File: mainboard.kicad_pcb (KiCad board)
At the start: 2 copper layers, 145 x 95 mm, 140 parts, among them J1 USB_C_Receptacle_USB2.0_16P, J10 Valve7, J11 AuxPump, J12 MainPump, J13 WaterLevelSensor, J14 OneWireTemp, J15 OneWireTemp, J2 Valve1, J3 Servo, J4 HX711, J5 Valve2, J6 Valve3, J7 Valve4, J8 Valve5, J9 Valve6, Q1 DMN3008SFG, Q10 IRLML2502, Q11 IRLML2502, Q2 DMN3008SFG, Q3 IRLML2502, Q4 IRLML2502, Q5 IRLML2502, Q6 IRLML2502, Q7 IRLML2502, Q8 IRLML2502, Q9 IRLML2502, SW1 SW_Push, SW2 SW_Push, SW3 SW_Push, U1 AP33771, U2 AP62150WU, U3 DRV8870DDAR, U4 AP62150WU, U5 USBLC6-2SC6, U6 ESP32-S3-WROOM-1

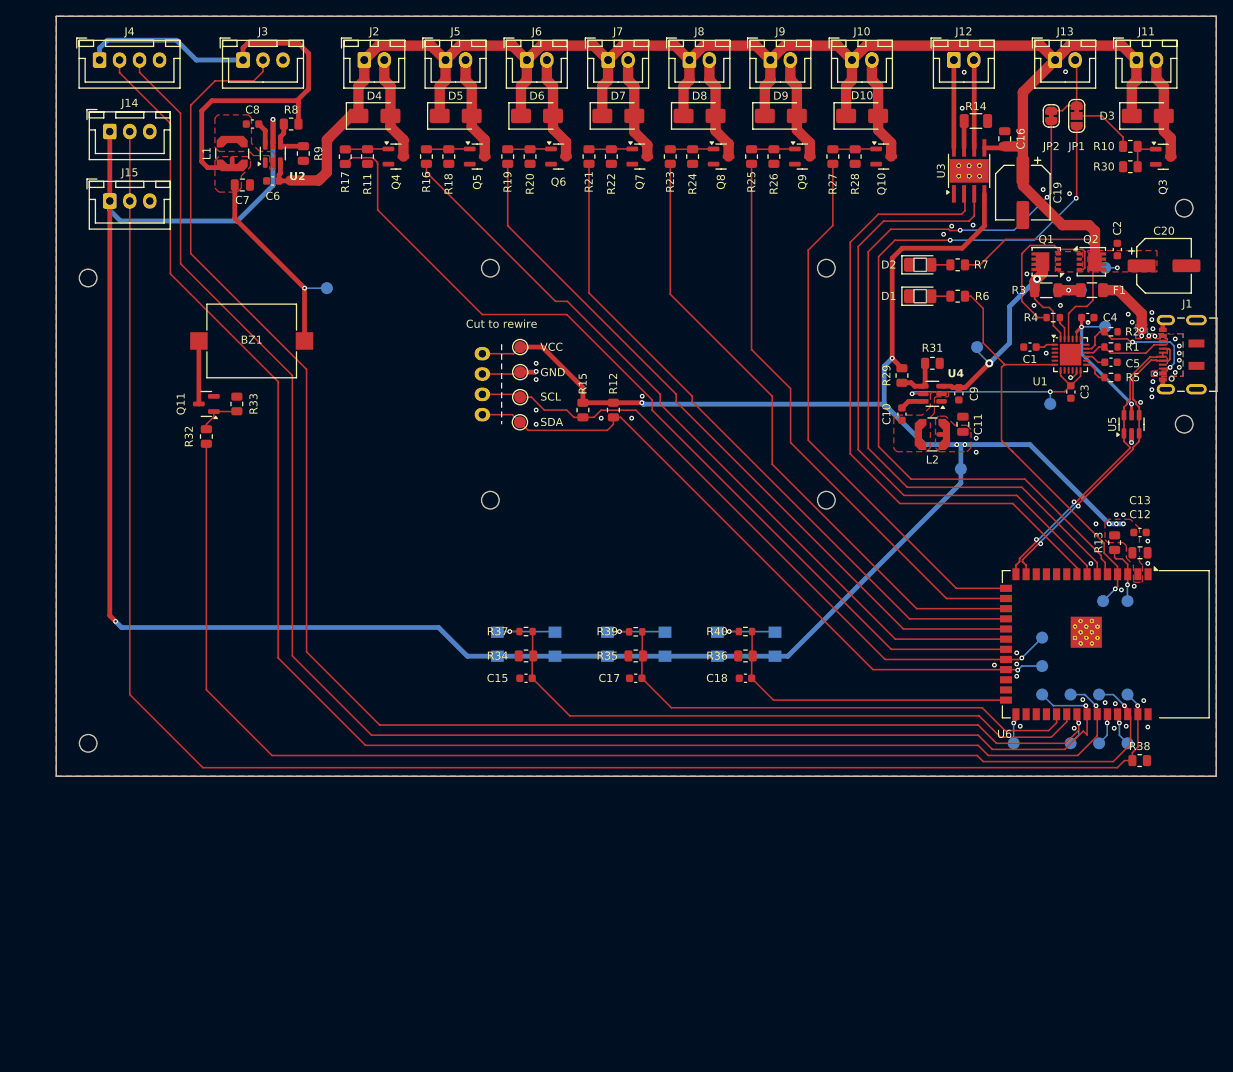
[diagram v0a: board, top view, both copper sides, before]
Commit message: Cleanup OLED stuff
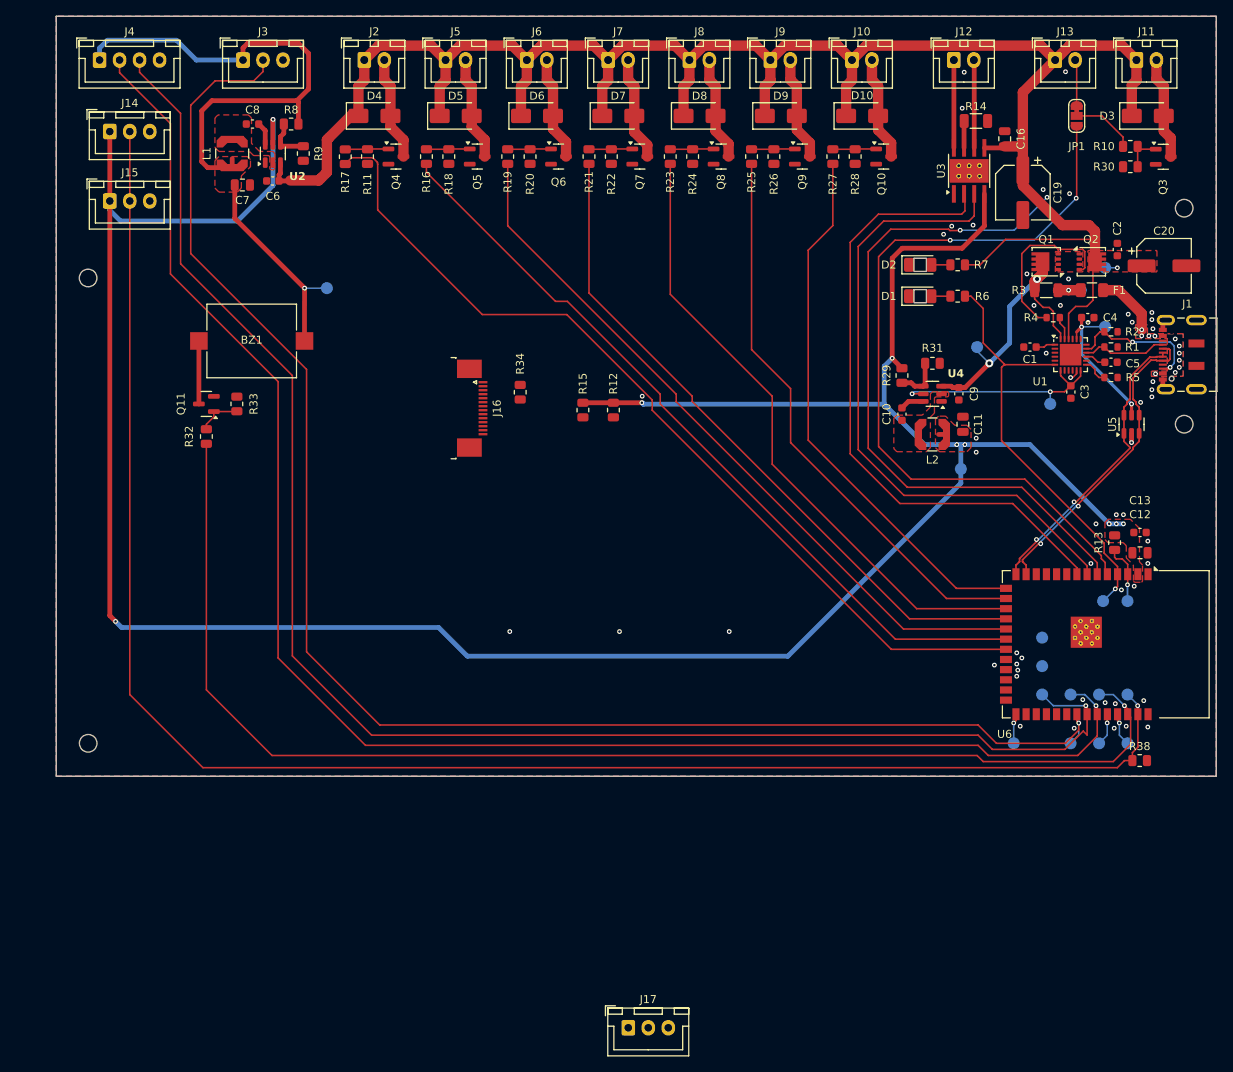
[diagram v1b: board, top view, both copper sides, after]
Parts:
- removed C15, C17, C18: 100n, Capacitor_SMD:C_0603_1608Metric
- removed JP2: SolderJumper_2_Bridged, Jumper:SolderJumper-2_P1.3mm_Bridged_RoundedPad1.0x1.5mm
- removed R35, R36: R100k, Resistor_SMD:R_0805_2012Metric
- removed R37, R39, R40: 1k, Resistor_SMD:R_0603_1608Metric
- removed SW1, SW2, SW3: SW_Push, Button_Switch_SMD:SW_SPST_TL3305A
- removed TP1, TP2, TP3, TP4: TestPoint_Small, TestPoint:TestPoint_Pad_D1.5mm
- removed U8: ~, project:OLED_1.5in_128x128
- added J16: Conn_01x14_MountingPin, Connector_FFC-FPC:TE_1-1734839-4_1x14-1MP_P0.5mm_Horizontal, F.Cu at (103.0, 78.0)
- added J17: FlowSensor, Connector_JST:JST_XH_B3B-XH-A_1x03_P2.50mm_Vertical, F.Cu at (122.5, 155.4)
- moved R34 33.0 mm to (109.0, 76.0), turned to -90 degrees
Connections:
- net /MCU/WATER_LEVEL_SENSOR renamed /Motor Control/WATER_LEVEL_SENSOR
- R12 pad 2: /MCU/OLED_SDA -> /MCU/LCD_TOUCH_SDA
- R15 pad 2: /MCU/OLED_SCL -> /MCU/LCD_TOUCH_SCL
- R34 pad 2: /MCU/BUTTON_1 -> /User Interface/LCD_CS
- TP7 pad 1: /MCU/OLED_SCL -> Net-(U6-IO14)
- TP8 pad 1: /MCU/OLED_SDA -> Net-(U6-IO21)
- U6 pad 22: /MCU/OLED_SCL -> Net-(U6-IO14)
- U6 pad 23: /MCU/OLED_SDA -> Net-(U6-IO21)
- U6 pad 26: /MCU/BUTTON_3 -> unconnected-(U6-IO45-Pad26)
- U6 pad 31: /MCU/BUTTON_2 -> unconnected-(U6-IO38-Pad31)
- U6 pad 32: /MCU/BUTTON_1 -> unconnected-(U6-IO39-Pad32)
- U6 pad 6: /MCU/WATER_LEVEL_SENSOR_PIN -> /MCU/FLOW_SENSOR
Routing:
- net /MCU/WATER_LEVEL_SENSOR_PIN: track 95.6 -> 0.00 mm, vias 2 -> 0
- net /MCU/FLOW_SENSOR: track 0.00 -> 85.9 mm, vias 0 -> 2
- net /MCU/OLED_SDA: track 85.3 -> 0.00 mm, vias 1 -> 0
- net /MCU/OLED_SCL: track 85.1 -> 0.00 mm, vias 1 -> 0
- net /MCU/BUTTON_1: track 77.2 -> 0.00 mm
- net /MCU/BUTTON_2: track 61.6 -> 0.00 mm
- net /MCU/BUTTON_3: track 38.5 -> 0.00 mm
- net +3.3V: track 348.1 -> 331.2 mm
- net Net-(R39-Pad1): track 8.25 -> 0.00 mm, vias 1 -> 0
- net Net-(R40-Pad1): track 8.24 -> 0.00 mm, vias 1 -> 0
- net Net-(R37-Pad1): track 8.24 -> 0.00 mm, vias 1 -> 0
- net GND: track 11.8 -> 5.28 mm, vias 56 -> 49
- net /Motor Control/WATER_LEVEL_SENSOR: track 8.94 -> 5.49 mm
- net (no net): vias 0 -> 5
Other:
- board text removed: "Check pinout!!!"
- board text removed: "Cut to rewire"
- board text removed: "GND"
- board text removed: "SCL"
- board text removed: "SDA"
- board text removed: "VCC"

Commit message: Cleanup
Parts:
- added TP1: TestPoint_Small, TestPoint:TestPoint_Pad_D1.5mm, F.Cu at (164.3, 150.4)
- added TP15: TestPoint_Small, TestPoint:TestPoint_Pad_D1.5mm, F.Cu at (171.4, 150.4)
- added TP2: TestPoint_Small, TestPoint:TestPoint_Pad_D1.5mm, F.Cu at (164.3, 154.0)
- added TP23: TestPoint_Small, TestPoint:TestPoint_Pad_D1.5mm, F.Cu at (171.4, 154.0)
- added TP24: TestPoint_Small, TestPoint:TestPoint_Pad_D1.5mm, F.Cu at (175.0, 150.4)
- added TP27: TestPoint_Small, TestPoint:TestPoint_Pad_D1.5mm, F.Cu at (175.0, 154.0)
- added TP3: TestPoint_Small, TestPoint:TestPoint_Pad_D1.5mm, F.Cu at (167.9, 150.4)
- added TP4: TestPoint_Small, TestPoint:TestPoint_Pad_D1.5mm, F.Cu at (167.9, 154.0)
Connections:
- J16 pad 7: /MCU/LCD_MISO -> /MCU/LCD_SCK
- J16 pad 8: /MCU/LCD_SCK -> /User Interface/LCD_BACKLIGHT
- J16 pad 9: /User Interface/LCD_LED_K -> /MCU/LCD_MISO
- TP7 pad 1: Net-(U6-IO14) -> /MCU/LCD_SCK
- TP8 pad 1: Net-(U6-IO21) -> /MCU/LCD_TOUCH_RESET
- U6 pad 10: unconnected-(U6-IO17-Pad10) -> /MCU/LCD_MOSI
- U6 pad 11: unconnected-(U6-IO18-Pad11) -> /MCU/LCD_MISO
- U6 pad 12: unconnected-(U6-IO8-Pad12) -> /MCU/LCD_RS
- U6 pad 22: Net-(U6-IO14) -> /MCU/LCD_SCK
- U6 pad 23: Net-(U6-IO21) -> /MCU/LCD_TOUCH_RESET
- U6 pad 26: unconnected-(U6-IO45-Pad26) -> /MCU/LCD_TOUCH_INT
- U6 pad 31: unconnected-(U6-IO38-Pad31) -> /MCU/LCD_TOUCH_SDA
- U6 pad 32: unconnected-(U6-IO39-Pad32) -> /MCU/LCD_TOUCH_SCL
- U6 pad 9: unconnected-(U6-IO16-Pad9) -> /MCU/LCD_RESET
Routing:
- net /MCU/HX711_CLK: track 199.0 -> 4.88 mm
- net /MCU/1WIRE_TEMP: track 208.9 -> 17.8 mm
- net /MCU/HX711_DAT: track 197.5 -> 7.17 mm
- net /MCU/SERVO_CTRL: track 193.5 -> 4.15 mm
- net /MCU/BUZZER: track 159.8 -> 4.99 mm
- net /MCU/VALVE1_CTRL: track 112.6 -> 0.00 mm
- net /MCU/VALVE2_CTRL: track 98.4 -> 0.00 mm
- net /MCU/VALVE3_CTRL: track 91.4 -> 0.00 mm
- net /MCU/VALVE4_CTRL: track 85.5 -> 0.00 mm
- net /MCU/MAIN_PUMP_CTRL1: track 79.9 -> 0.00 mm
- net /MCU/VALVE5_CTRL: track 79.5 -> 0.00 mm
- net /MCU/MAIN_PUMP_CTRL2: track 79.5 -> 0.00 mm
- net /MCU/FLOW_SENSOR: track 85.9 -> 12.6 mm
- net /MCU/VALVE6_CTRL: track 71.9 -> 0.00 mm
- net /MCU/AUX_PUMP_CTRL: track 96.2 -> 26.9 mm
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
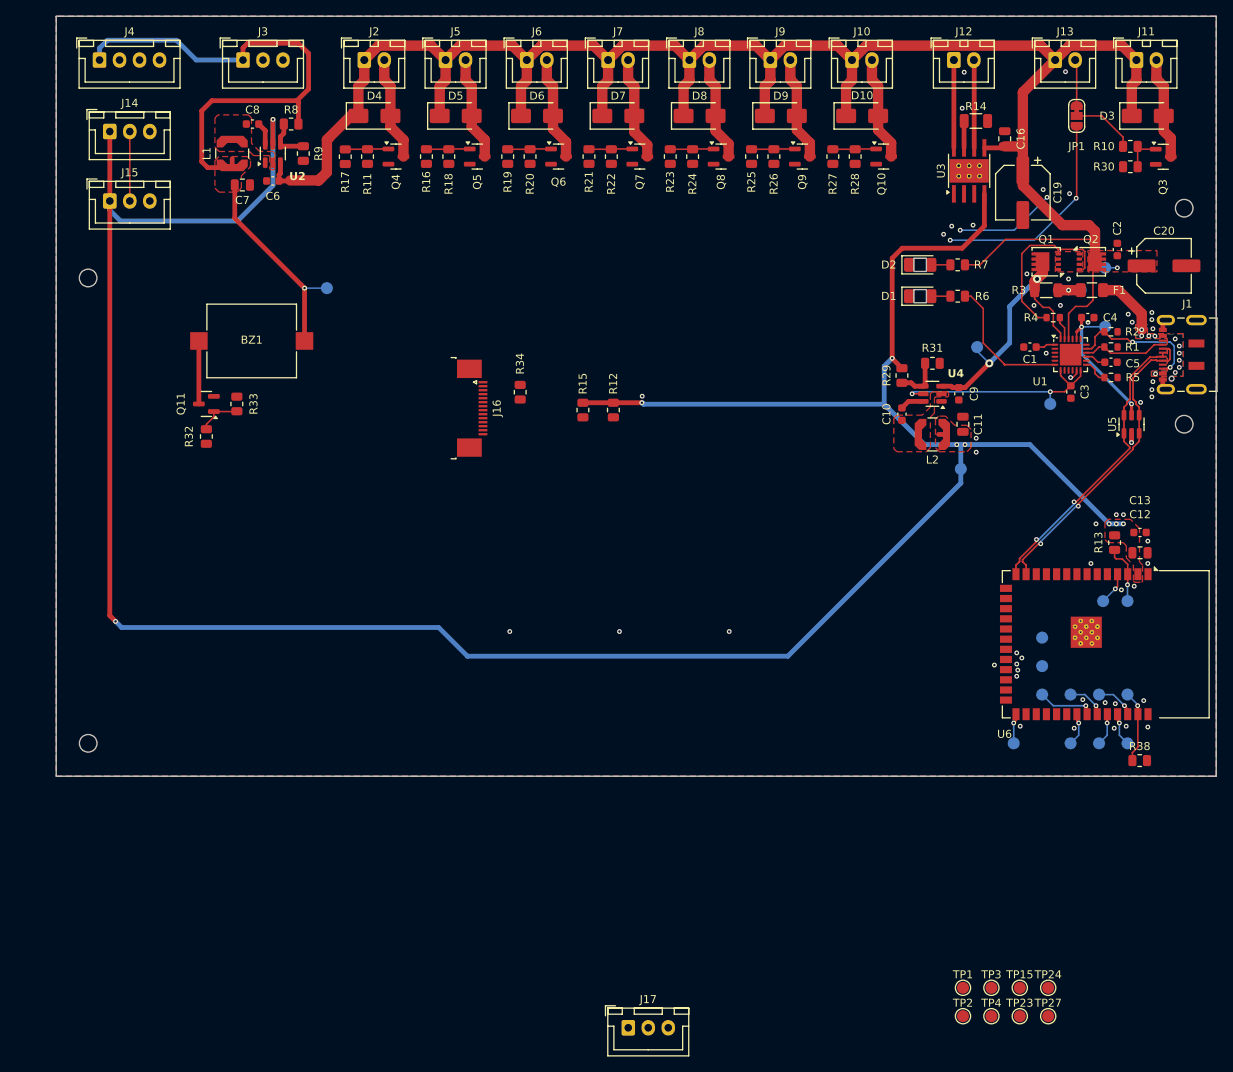
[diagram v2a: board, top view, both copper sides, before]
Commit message: Work on improving USB & power layout
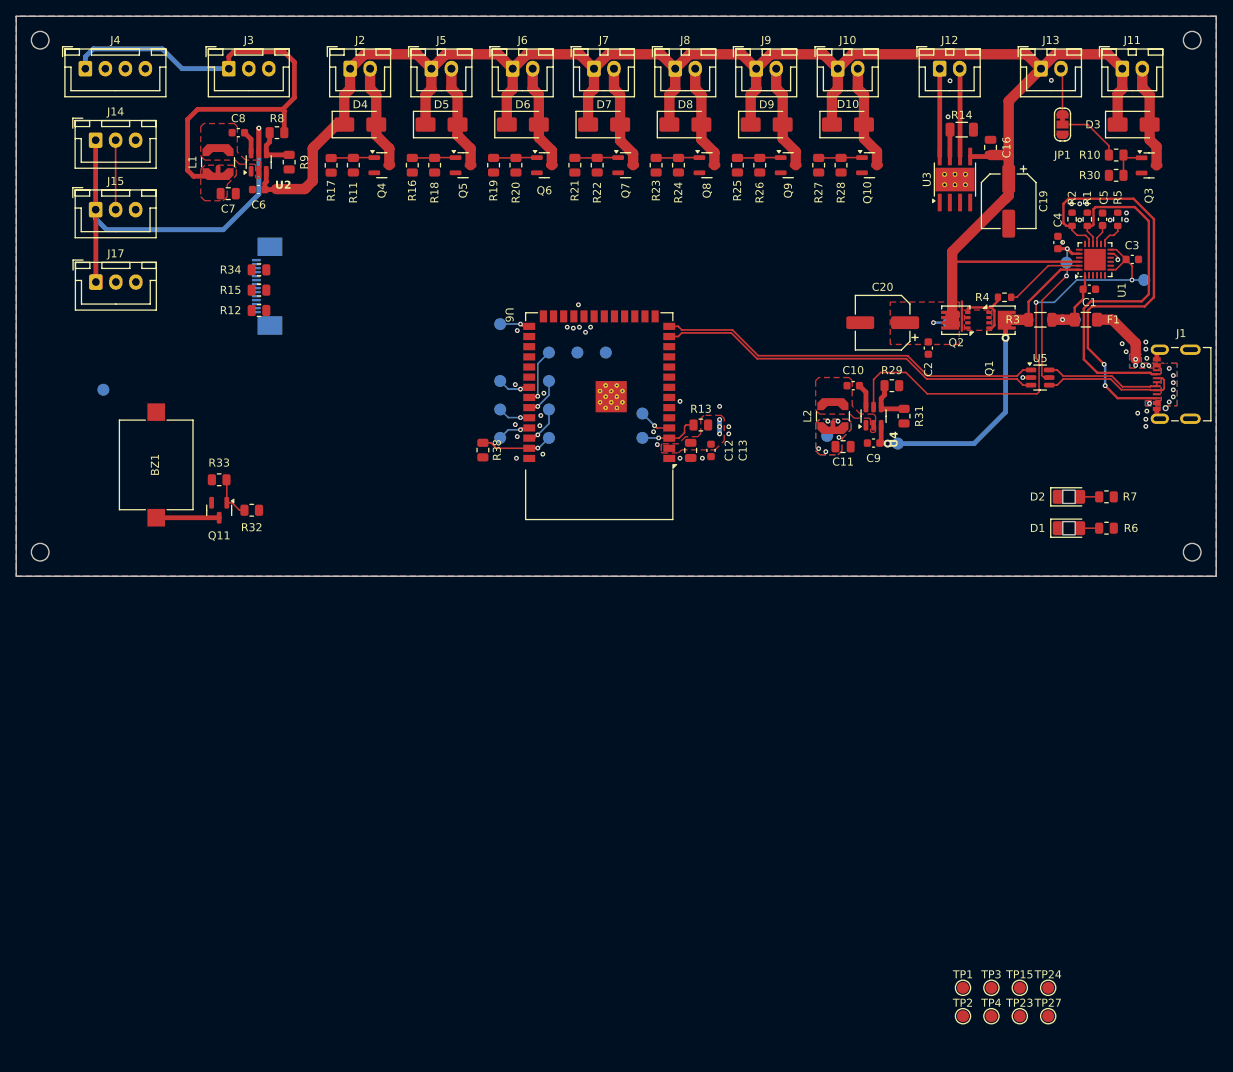
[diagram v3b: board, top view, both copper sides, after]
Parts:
- J16: moved to B.Cu
- moved J17 114.5 mm to (56.0, 62.2)
- moved R38 90.8 mm to (104.3, 83.2), turned to 90 degrees
- moved TP17 87.2 mm to (106.5, 81.7), turned to 90 degrees
- moved TP16 85.7 mm to (106.5, 78.2), turned to -90 degrees
- moved TP10 84.5 mm to (106.5, 74.6), turned to 90 degrees
- moved TP6 82.9 mm to (106.5, 67.5), turned to -90 degrees
- moved TP14 79.1 mm to (112.6, 81.7), turned to 90 degrees
- moved TP13 77.4 mm to (112.6, 78.2), turned to -90 degrees
- moved TP11 76.1 mm to (112.6, 74.6), turned to 90 degrees
- moved TP12 75.0 mm to (112.6, 71.0), turned to -90 degrees
- moved TP8 70.1 mm to (116.1, 71.0), turned to 180 degrees
- moved U6 69.5 mm to (118.9, 79.0), turned to 180 degrees
- moved TP7 65.1 mm to (119.7, 71.0), turned to 180 degrees
- moved TP5 64.0 mm to (124.3, 81.7), turned to -90 degrees
- moved TP9 62.2 mm to (124.3, 78.7), turned to 90 degrees
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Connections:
- J1 pad A6: /MCU/USB_D+ -> /Power/USB_EXT_D+
- J1 pad A7: /MCU/USB_D- -> /Power/USB_EXT_D-
- J1 pad B6: /MCU/USB_D+ -> /Power/USB_EXT_D+
- J1 pad B7: /MCU/USB_D- -> /Power/USB_EXT_D-
- U5 pad 4: /MCU/USB_D- -> /Power/USB_EXT_D-
- U5 pad 6: /MCU/USB_D+ -> /Power/USB_EXT_D+
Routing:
- net +3.3V: track 331.2 -> 55.9 mm
- net /Power/CC1: track 17.1 -> 56.1 mm
- net /Power/CC2: track 10.6 -> 47.3 mm
- net /Power/V3VD: track 28.0 -> 59.5 mm
- net /MCU/AUX_PUMP_CTRL: track 26.9 -> 0.00 mm, vias 2 -> 0
- net +5V: track 90.8 -> 64.9 mm, vias 1 -> 0
- net /Power/FAULT: track 21.6 -> 4.10 mm
- net /Power/USB_EXT_D-: track 0.00 -> 17.4 mm
- net /Power/USB_EXT_D+: track 0.00 -> 14.8 mm
- net /Power/PWR_EN_GATE: track 21.9 -> 8.30 mm
- net /MCU/FLOW_SENSOR: track 12.6 -> 0.00 mm, vias 2 -> 0
- net /MCU/USB_D+: track 37.2 -> 48.1 mm, vias 2 -> 0
- net /Power/PWR_VCC: track 34.3 -> 44.5 mm
- net +15V: track 252.6 -> 243.3 mm
- net /MCU/USB_D-: track 39.2 -> 48.1 mm, vias 2 -> 0
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- added copper zone on B.Cu, net +3.3V
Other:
- board size 145 x 95 mm -> 150 x 70 mm
